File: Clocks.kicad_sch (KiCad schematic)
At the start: 11 parts, among them U652 CDCLVC1106, Y601 588S160X2CAT, Y602 ECS-TXO-2016-33-160-TR

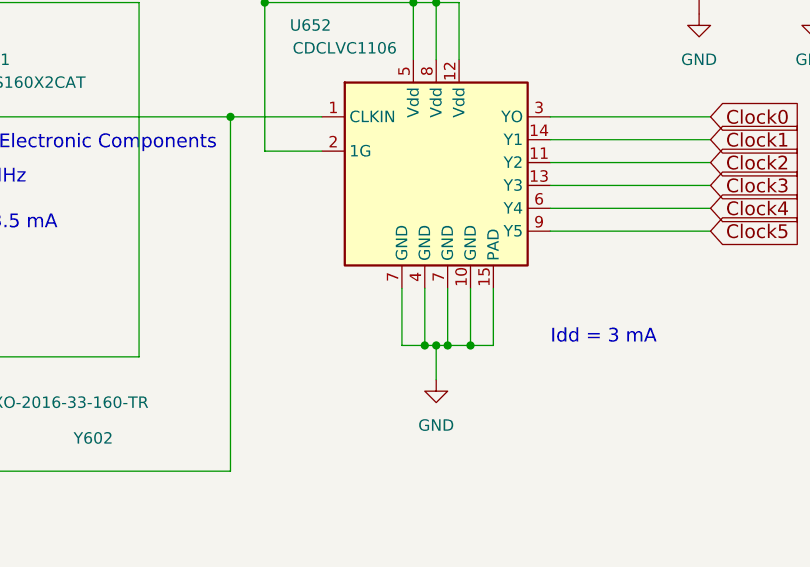
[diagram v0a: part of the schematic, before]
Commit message: Lots of cleanups to fix numerous issues
Signed-off-by: Corey Minyard <corey@minyard.net>
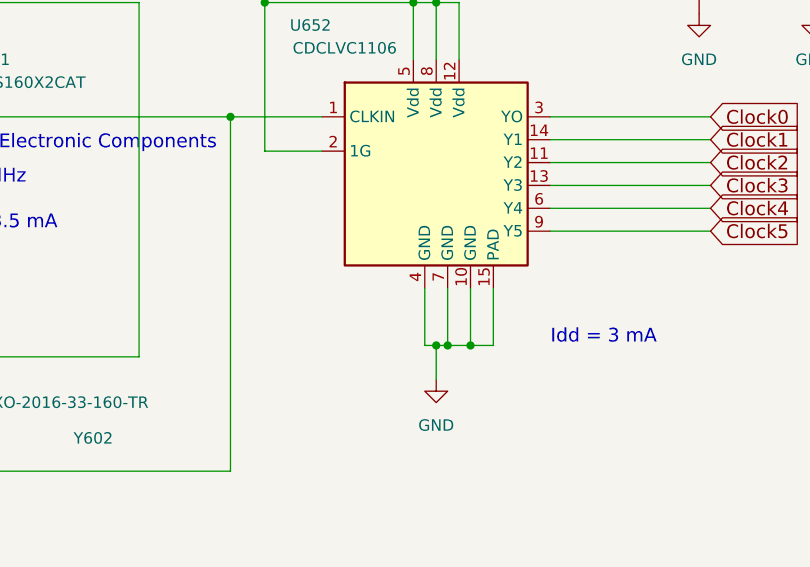
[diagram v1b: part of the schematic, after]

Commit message: Finish up most of the ax5043 routing
Signed-off-by: Corey Minyard <corey@minyard.net>
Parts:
- U652: footprint Package_SO:HTSSOP-14-1EP_4.4x5mm_P0.65mm_EP3.4x5mm_Mask3x3.1mm -> Package_SO:Texas_HTSSOP-14-1EP_4.4x5mm_P0.65mm_EP3.4x5mm_Mask3.155x3.255mm
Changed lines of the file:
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@@
 			)
 		)
-		(property "Footprint" "Package_SO:HTSSOP-14-1EP_4.4x5mm_P0.65mm_EP3.4x5mm_Mask3x3.1mm"
+		(property "Footprint" "Package_SO:Texas_HTSSOP-14-1EP_4.4x5mm_P0.65mm_EP3.4x5mm_Mask3.155x3.255mm"
 			(at 201.93 113.03 0)
 			(effects

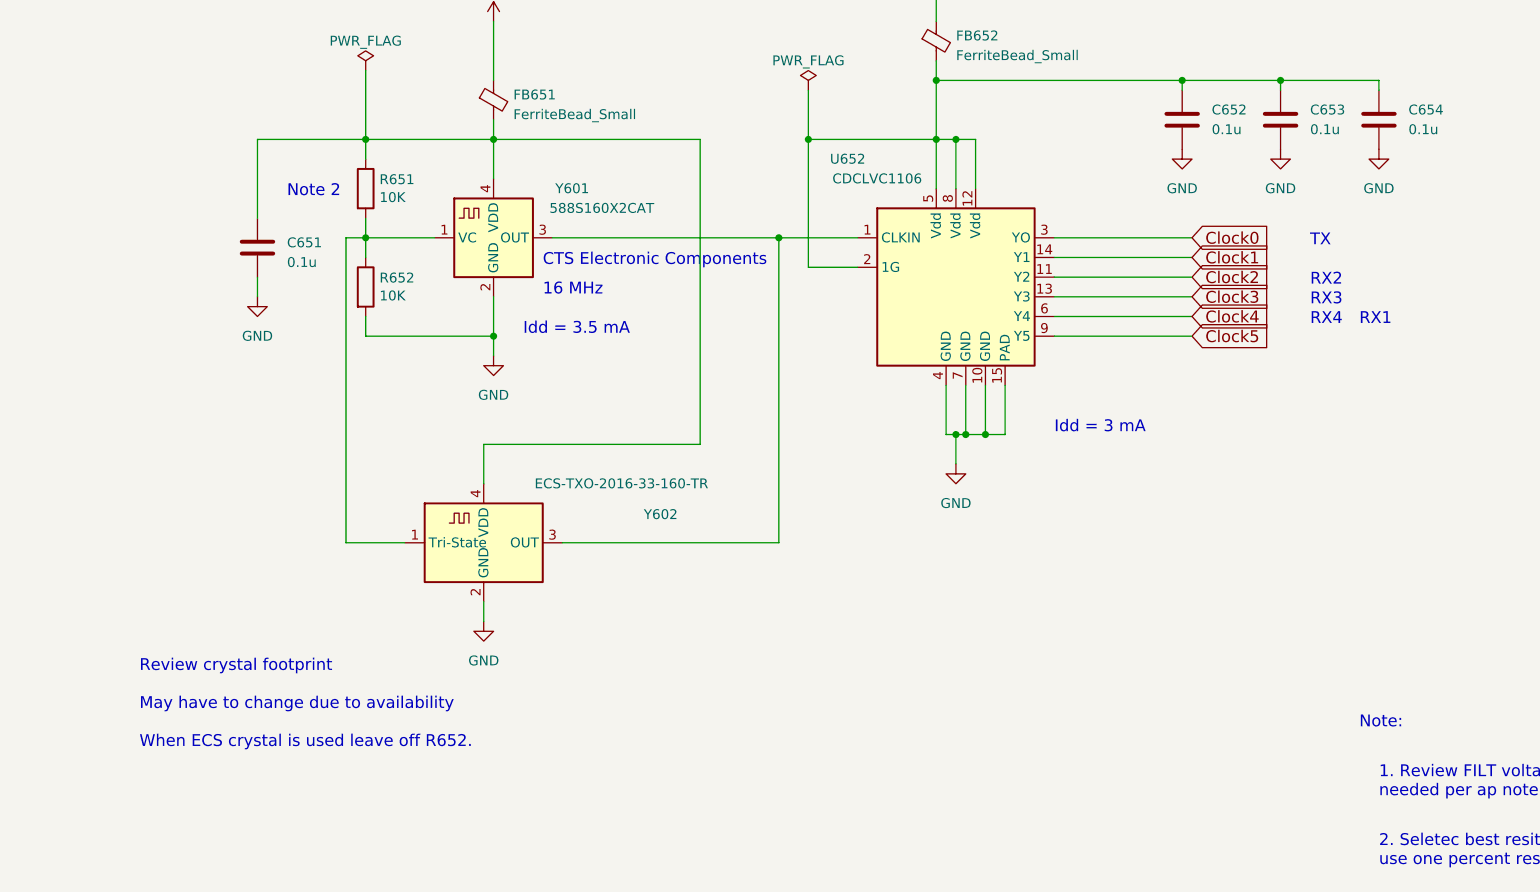
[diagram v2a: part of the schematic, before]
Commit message: Wire in clocks, more cleanups, wire in MRAM
Signed-off-by: Corey Minyard <corey@minyard.net>
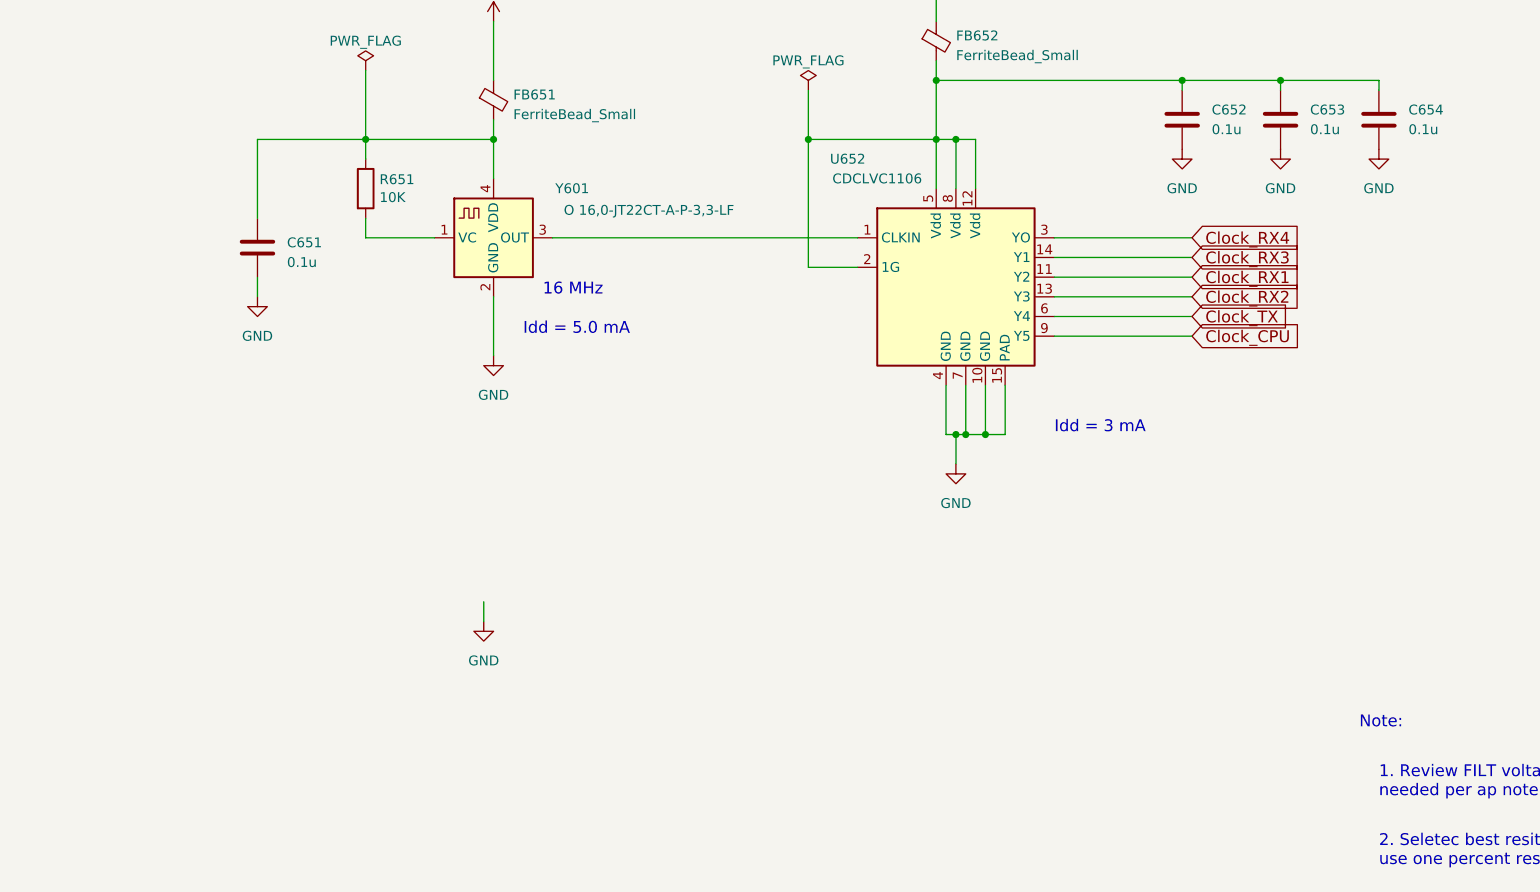
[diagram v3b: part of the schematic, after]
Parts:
- removed R652: 10K, Resistor_SMD:R_0603_1608Metric_Pad0.98x0.95mm_HandSolder, symbol Device:R
- removed Y602: ECS-TXO-2016-33-160-TR, Oscillator:Oscillator_SMD_ECS_2520MV-xxx-xx-4Pin_2.5x2.0mm, symbol Oscillator:ECS-2520MV-xxx-xx
- Y601: value 588S160X2CAT -> O 16,0-JT22CT-A-P-3,3-LF; footprint PacSatDev_misc:Oscillator_SMD_CTS_4X5mm -> Oscillator:Oscillator_SMD_SiT_PQFN-4Pin_2.5x2.0mm
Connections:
- net Clock0 renamed Clock_RX4
- net Clock1 renamed Clock_RX3
- net Clock2 renamed Clock_RX1
- net Clock3 renamed Clock_RX2
- net Clock4 renamed Clock_TX
- net Clock5 renamed Clock_CPU
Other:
- note added: "Idd = 5.0 mA"
- note removed: "CTS Electronic Components"
- note removed: "Idd = 3.5 mA"
- note removed: "Note 2"
- note removed: "RX1"
- note removed: "RX2"
- note removed: "RX3"
- note removed: "RX4"
- note removed: "Review crystal footprint May have to change due to availability When ECS crystal is used leave off R652."
- note removed: "TX"

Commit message: Finish up and clean up a lot of things
Signed-off-by: Corey Minyard <corey@minyard.net>
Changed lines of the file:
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@@
-	(wire
-		(pts
-			(xy 154.94 153.67) (xy 154.94 156.21)
-		)
-		(stroke
-			(width 0)
-			(type default)
-		)
-	)
 	(wire
 		(pts
@@
 					(unit 1)
 				)
-			)
-		)
-	)
-	(symbol
-		(lib_id "power:GND")
-		(at 154.94 156.21 0)
-		(unit 1)
-		(exclude_from_sim no)
-		(in_bom yes)
-		(on_board yes)
-		(dnp no)
-		(fields_autoplaced yes)
-		(property "Reference" "#PWR0143"
-			(at 154.94 162.56 0)
-			(effects
-				(font
-					(size 1.27 1.27)
-				)
-				(hide yes)
-			)
-		)
-		(property "Value" "GND"
-			(at 154.94 161.29 0)
-			(effects
-				(font
-					(size 1.27 1.27)
-				)
-			)
-		)
-		(property "Footprint" ""
-			(at 154.94 156.21 0)
-			(effects
-				(font
-					(size 1.27 1.27)
-				)
-				(hide yes)
-			)
-		)
-		(property "Datasheet" ""
-			(at 154.94 156.21 0)
-			(effects
-				(font
-					(size 1.27 1.27)
-				)
-				(hide yes)
-			)
-		)
-		(property "Description" ""
-			(at 154.94 156.21 0)
-			(effects
-				(font
-					(size 1.27 1.27)
-				)
-			)
-		)
-		(pin "1"
-		)
-		(instances
-			(project "PacSat_Dev_RevD_240614"
-				(path "/cc9f42d2-6985-41ac-acab-5ab7b01c5b38/a735fef7-c3fa-4339-b3a6-fbce810c3c4b"
-					(reference "#PWR0143")
-					(unit 1)
-				)

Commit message: Re-annotate all parts
And get rid of the per-sheet annotation remarks.

Signed-off-by: Corey Minyard <corey@minyard.net>
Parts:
- renumbered C651 to C23, C652 to C24, C653 to C25, C654 to C26, FB651 to FB2, FB652 to FB3, R651 to R25, U652 to U3, Y601 to Y2
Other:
- note removed: "Symbol Numbers 650 up"
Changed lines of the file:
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@@
-		)
-	)
-	(text "Symbol Numbers 650 up"
-		(exclude_from_sim no)
-		(at 30.48 243.84 0)
-		(effects
-			(font
-				(size 1.27 1.27)
-			)
-			(justify left bottom)
 		)
 	)
@@
 		(dnp no)
 		(fields_autoplaced yes)
-		(property "Reference" "C652"
+		(property "Reference" "C24"
 			(at 248.92 90.1699 0)
 			(effects
@@
 			(project "PacSat_Dev_RevD_240614"
 				(path "/cc9f42d2-6985-41ac-acab-5ab7b01c5b38/a735fef7-c3fa-4339-b3a6-fbce810c3c4b"
-					(reference "C652")
+					(reference "C24")
 					(unit 1)
 				)
@@
 		(dnp no)
 		(fields_autoplaced yes)
-		(property "Reference" "#PWR0655"
+		(property "Reference" "#PWR055"
 			(at 215.9 142.24 0)
 			(effects
@@
 			(project "PacSat_Dev_RevD_240614"
 				(path "/cc9f42d2-6985-41ac-acab-5ab7b01c5b38/a735fef7-c3fa-4339-b3a6-fbce810c3c4b"
-					(reference "#PWR0655")
+					(reference "#PWR055")
 					(unit 1)
 				)
@@
 		(dnp no)
 		(fields_autoplaced yes)
-		(property "Reference" "#PWR0652"
+		(property "Reference" "#PWR052"
 			(at 156.21 82.55 0)
 			(effects
@@
 			(project "PacSat_Dev_RevD_240614"
 				(path "/cc9f42d2-6985-41ac-acab-5ab7b01c5b38/a735fef7-c3fa-4339-b3a6-fbce810c3c4b"
-					(reference "#PWR0652")
+					(reference "#PWR052")
 					(unit 1)
 				)
@@
 		(dnp no)
 		(fields_autoplaced yes)
-		(property "Reference" "FB651"
+		(property "Reference" "FB2"
 			(at 158.75 88.2269 0)
 			(effects
@@
 			(project "PacSat_Dev_RevD_240614"
 				(path "/cc9f42d2-6985-41ac-acab-5ab7b01c5b38/a735fef7-c3fa-4339-b3a6-fbce810c3c4b"
-					(reference "FB651")
+					(reference "FB2")
 					(unit 1)
 				)
@@
 		(dnp no)
 		(fields_autoplaced yes)
-		(property "Reference" "#PWR0658"
+		(property "Reference" "#PWR058"
 			(at 270.51 101.6 0)
 			(effects
@@
 			(project "PacSat_Dev_RevD_240614"
 				(path "/cc9f42d2-6985-41ac-acab-5ab7b01c5b38/a735fef7-c3fa-4339-b3a6-fbce810c3c4b"
-					(reference "#PWR0658")
+					(reference "#PWR058")
 					(unit 1)
 				)
@@
 		(dnp no)
 		(fields_autoplaced yes)
-		(property "Reference" "#PWR0657"
+		(property "Reference" "#PWR057"
 			(at 257.81 101.6 0)
 			(effects
@@
 			(project "PacSat_Dev_RevD_240614"
 				(path "/cc9f42d2-6985-41ac-acab-5ab7b01c5b38/a735fef7-c3fa-4339-b3a6-fbce810c3c4b"
-					(reference "#PWR0657")
+					(reference "#PWR057")
 					(unit 1)
 				)
@@
 		(dnp no)
 		(fields_autoplaced yes)
-		(property "Reference" "#FLG095"
+		(property "Reference" "#FLG03"
 			(at 196.85 85.725 0)
 			(effects
@@
 			(project "PacSat_Dev_RevD_240614"
 				(path "/cc9f42d2-6985-41ac-acab-5ab7b01c5b38/a735fef7-c3fa-4339-b3a6-fbce810c3c4b"
-					(reference "#FLG095")
+					(reference "#FLG03")
 					(unit 1)
 				)
@@
 		(dnp no)
 		(fields_autoplaced yes)
-		(property "Reference" "#FLG06"
+		(property "Reference" "#FLG02"
 			(at 139.7 83.185 0)
 			(effects
@@
 			(project "PacSat_Dev_RevD_240614"
 				(path "/cc9f42d2-6985-41ac-acab-5ab7b01c5b38/a735fef7-c3fa-4339-b3a6-fbce810c3c4b"
-					(reference "#FLG06")
+					(reference "#FLG02")
 					(unit 1)
 				)
@@
 		(dnp no)
 		(fields_autoplaced yes)
-		(property "Reference" "#PWR0654"
+		(property "Reference" "#PWR054"
 			(at 213.36 76.2 0)
 			(effects
@@
 			(project "PacSat_Dev_RevD_240614"
 				(path "/cc9f42d2-6985-41ac-acab-5ab7b01c5b38/a735fef7-c3fa-4339-b3a6-fbce810c3c4b"
-					(reference "#PWR0654")
+					(reference "#PWR054")
 					(unit 1)
 				)
@@
 		(on_board yes)
 		(dnp no)
-		(property "Reference" "R651"
+		(property "Reference" "R25"
 			(at 141.478 99.1616 0)
 			(effects
@@
 			(project "PacSat_Dev_RevD_240614"
 				(path "/cc9f42d2-6985-41ac-acab-5ab7b01c5b38/a735fef7-c3fa-4339-b3a6-fbce810c3c4b"
-					(reference "R651")
+					(reference "R25")
 					(unit 1)
 				)
@@
 		(dnp no)
 		(fields_autoplaced yes)
-		(property "Reference" "#PWR0656"
+		(property "Reference" "#PWR056"
 			(at 245.11 101.6 0)
 			(effects
@@
 			(project "PacSat_Dev_RevD_240614"
 				(path "/cc9f42d2-6985-41ac-acab-5ab7b01c5b38/a735fef7-c3fa-4339-b3a6-fbce810c3c4b"
-					(reference "#PWR0656")
+					(reference "#PWR056")
 					(unit 1)
 				)
@@
 		(dnp no)
 		(fields_autoplaced yes)
-		(property "Reference" "FB652"
+		(property "Reference" "FB3"
 			(at 215.9 80.6069 0)
 			(effects
@@
 			(project "PacSat_Dev_RevD_240614"
 				(path "/cc9f42d2-6985-41ac-acab-5ab7b01c5b38/a735fef7-c3fa-4339-b3a6-fbce810c3c4b"
-					(reference "FB652")
+					(reference "FB3")
 					(unit 1)
 				)
@@
 		(dnp no)
 		(fields_autoplaced yes)
-		(property "Reference" "C651"
+		(property "Reference" "C23"
 			(at 129.54 107.315 0)
 			(effects
@@
 			(project "PacSat_Dev_RevD_240614"
 				(path "/cc9f42d2-6985-41ac-acab-5ab7b01c5b38/a735fef7-c3fa-4339-b3a6-fbce810c3c4b"
-					(reference "C651")
+					(reference "C23")
 					(unit 1)
 				)
@@
 		(on_board yes)
 		(dnp no)
-		(property "Reference" "Y601"
+		(property "Reference" "Y2"
 			(at 166.37 100.33 0)
 			(effects
@@
 			(project "PacSat_Dev_RevD_240614"
 				(path "/cc9f42d2-6985-41ac-acab-5ab7b01c5b38/a735fef7-c3fa-4339-b3a6-fbce810c3c4b"
-					(reference "Y601")
+					(reference "Y2")
 					(unit 1)
 				)
@@
 		(dnp no)
 		(fields_autoplaced yes)
-		(property "Reference" "#PWR0653"
+		(property "Reference" "#PWR053"
 			(at 156.21 128.27 0)
 			(effects
@@
 			(project "PacSat_Dev_RevD_240614"
 				(path "/cc9f42d2-6985-41ac-acab-5ab7b01c5b38/a735fef7-c3fa-4339-b3a6-fbce810c3c4b"
-					(reference "#PWR0653")
+					(reference "#PWR053")
 					(unit 1)
 				)
@@
 		(dnp no)
 		(fields_autoplaced yes)
-		(property "Reference" "C653"
+		(property "Reference" "C25"
 			(at 261.62 90.1699 0)
 			(effects
@@
 			(project "PacSat_Dev_RevD_240614"
 				(path "/cc9f42d2-6985-41ac-acab-5ab7b01c5b38/a735fef7-c3fa-4339-b3a6-fbce810c3c4b"
-					(reference "C653")
+					(reference "C25")
 					(unit 1)
 				)
@@
 		(on_board yes)
 		(dnp no)
-		(property "Reference" "U652"
+		(property "Reference" "U3"
 			(at 201.93 96.52 0)
 			(effects
@@
 			(project "PacSat_Dev_RevD_240614"
 				(path "/cc9f42d2-6985-41ac-acab-5ab7b01c5b38/a735fef7-c3fa-4339-b3a6-fbce810c3c4b"
-					(reference "U652")
+					(reference "U3")
 					(unit 1)
 				)
@@
 		(dnp no)
 		(fields_autoplaced yes)
-		(property "Reference" "C654"
+		(property "Reference" "C26"
 			(at 274.32 90.1699 0)
 			(effects
@@
 			(project "PacSat_Dev_RevD_240614"
 				(path "/cc9f42d2-6985-41ac-acab-5ab7b01c5b38/a735fef7-c3fa-4339-b3a6-fbce810c3c4b"
-					(reference "C654")
+					(reference "C26")
 					(unit 1)
 				)
@@
 		(dnp no)
 		(fields_autoplaced yes)
-		(property "Reference" "#PWR0651"
+		(property "Reference" "#PWR051"
 			(at 125.73 120.65 0)
 			(effects
@@
 			(project "PacSat_Dev_RevD_240614"
 				(path "/cc9f42d2-6985-41ac-acab-5ab7b01c5b38/a735fef7-c3fa-4339-b3a6-fbce810c3c4b"
-					(reference "#PWR0651")
+					(reference "#PWR051")
 					(unit 1)
 				)

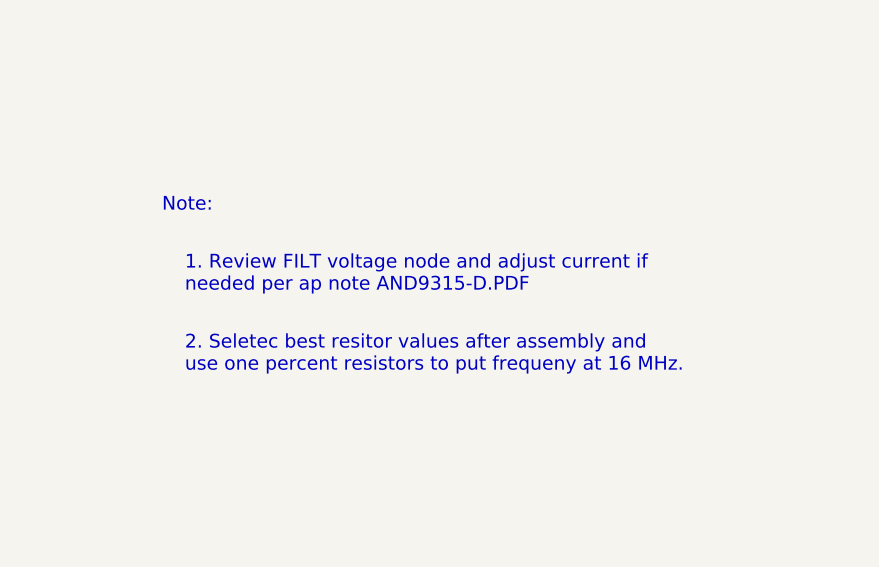
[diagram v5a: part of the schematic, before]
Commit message: Check over notes and some component values
Fix a wrong capacitor in one spot, set Q and voltage as necessary.

Signed-off-by: Corey Minyard <corey@minyard.net>
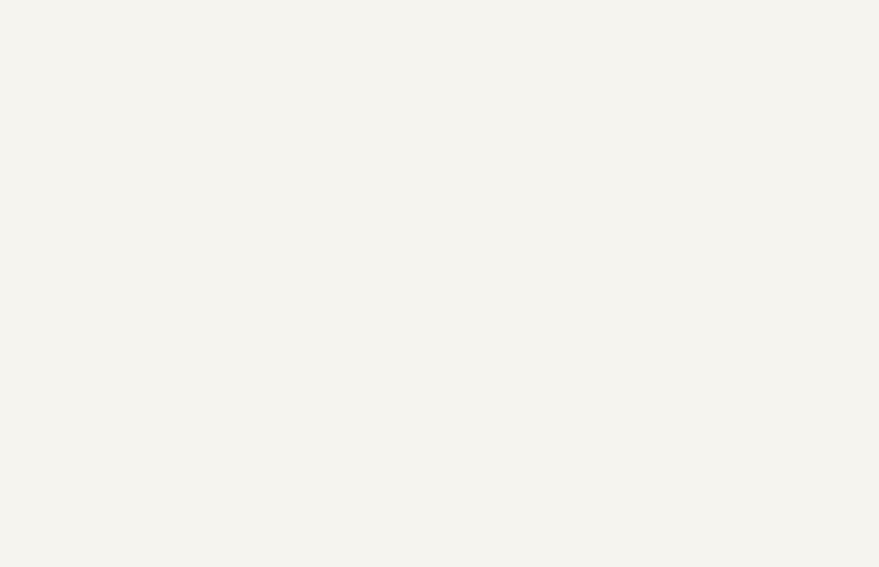
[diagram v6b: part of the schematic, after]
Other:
- note removed: "1. Review FILT voltage node and adjust current if needed per ap note AND9315-D.PDF"
- note removed: "2. Seletec best resitor values after assembly and use one percent resistors to put frequeny at 16 MHz."
- note removed: "Note:"
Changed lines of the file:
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@@
 		(comment 1 "N5BRG")
-	)
-	(text "1. Review FILT voltage node and adjust current if\nneeded per ap note AND9315-D.PDF"
-		(exclude_from_sim no)
-		(at 270.51 179.07 0)
-		(effects
-			(font
-				(size 1.524 1.524)
-			)
-			(justify left bottom)
-		)
 	)
 	(text "CLOCK"
 		(exclude_from_sim no)
 		(at 336.55 246.38 0)
-		(effects
-			(font
-				(size 1.524 1.524)
-			)
-			(justify left bottom)
-		)
-	)
-	(text "Note:\n"
-		(exclude_from_sim no)
-		(at 267.97 170.18 0)
 		(effects
 			(font
@@
 		(effects
 			(font
-				(size 1.524 1.524)
-			)
-			(justify left bottom)
-		)
-	)
-	(text "2. Seletec best resitor values after assembly and\nuse one percent resistors to put frequeny at 16 MHz."
-		(exclude_from_sim no)
-		(at 270.51 187.96 0)
-		(effects
-			(font
